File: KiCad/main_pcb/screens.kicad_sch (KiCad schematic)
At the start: 23 parts, among them U11 TI TXB0104DR, U12 ILI9488, U13 TI TXB0104DR, U14 SD Card Socket, U16 TI TXB0104DR

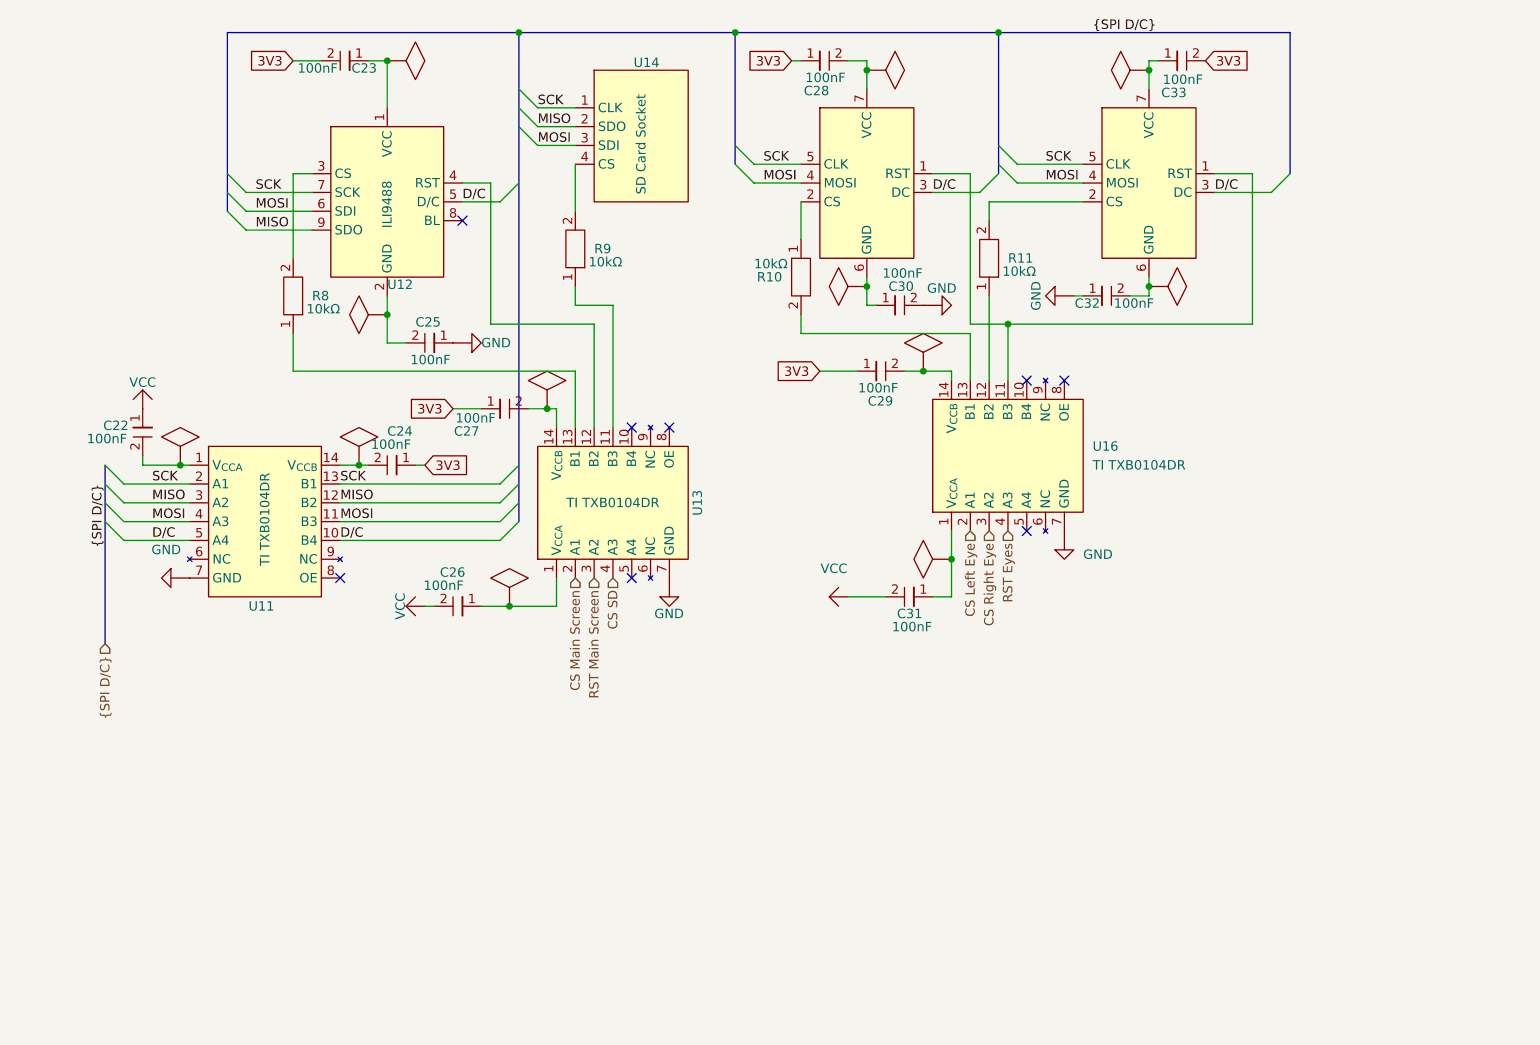
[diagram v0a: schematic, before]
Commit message: feat(KiCad): Adds parallel condensators for USB-C VBUS pin
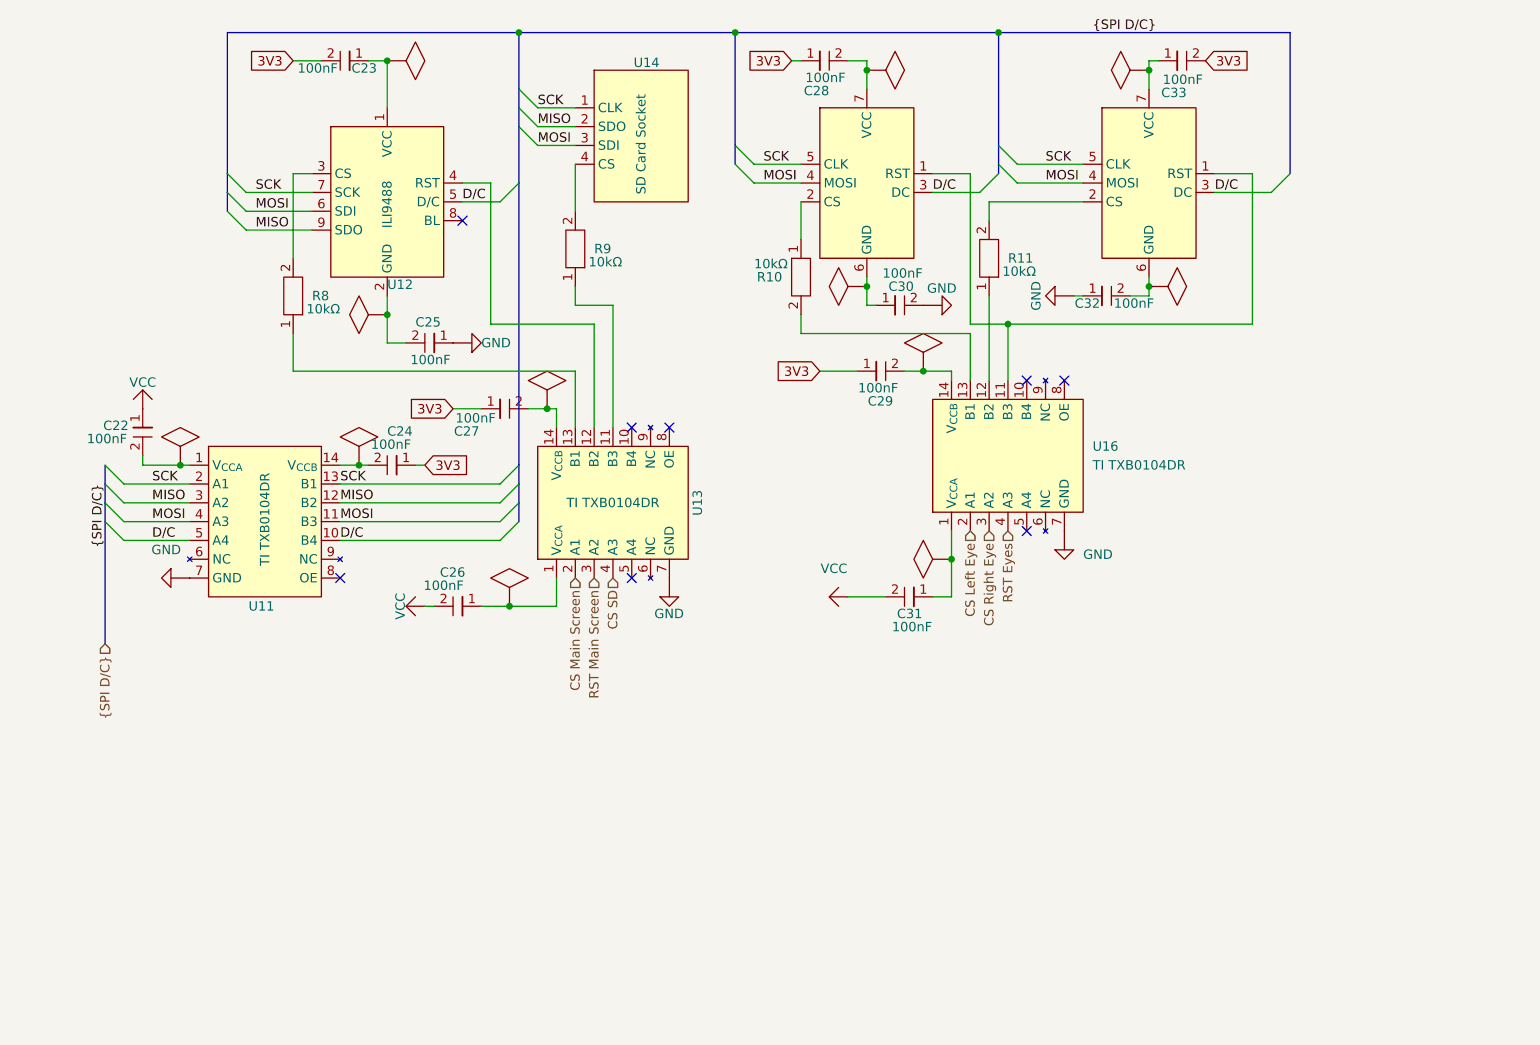
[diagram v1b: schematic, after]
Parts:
- U15, U17: value (none) -> ~

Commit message: feat(KiCad): Fixes symbols and ERC
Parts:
- C22, C23, C24, C25, C26, C27, C28, C29, C30, C31, C32, C33: symbol lilys_pad:Capacitor -> Lily's Pad:Capacitor
- R10, R11, R8, R9: symbol lilys_pad:Resistor -> Lily's Pad:Resistor
- U11, U13, U16: symbol lilys_pad:TI_TXB0104DR -> Lily's Pad:TI_TXB0104DR
- U12: symbol lilys_pad:ILI9488 -> Lily's Pad:ILI9488
- U14: symbol lilys_pad:SD_Card_Socket -> Lily's Pad:SD_Card_Socket
- U15, U17: symbol lilys_pad:GC9A01 -> Lily's Pad:GC9A01
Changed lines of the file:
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@@
 	)
 	(symbol
-		(lib_id "lilys_pad:Resistor")
+		(lib_id "Lily's Pad:Resistor")
 		(at 99.06 54.61 180)
 		(unit 1)
@@
 	)
 	(symbol
-		(lib_id "lilys_pad:PWR_FLG")
+		(lib_id "Lily's Pad:PWR_FLG")
 		(at 95.25 73.66 180)
 		(unit 1)
@@
 	)
 	(symbol
-		(lib_id "lilys_pad:Capacitor")
+		(lib_id "Lily's Pad:Capacitor")
 		(at 140.97 71.12 90)
 		(unit 1)
@@
 	)
 	(symbol
-		(lib_id "lilys_pad:GND")
+		(lib_id "Lily's Pad:GND")
 		(at 111.76 101.6 0)
 		(unit 1)
@@
 	)
 	(symbol
-		(lib_id "lilys_pad:Capacitor")
+		(lib_id "Lily's Pad:Capacitor")
 		(at 73.66 83.82 270)
 		(unit 1)
@@
 	)
 	(symbol
-		(lib_id "lilys_pad:PWR_FLG")
+		(lib_id "Lily's Pad:PWR_FLG")
 		(at 45.72 81.28 180)
 		(unit 1)
@@
 	)
 	(symbol
-		(lib_id "lilys_pad:TI_TXB0104DR")
+		(lib_id "Lily's Pad:TI_TXB0104DR")
 		(at 157.48 82.55 90)
 		(unit 1)
@@
 	)
 	(symbol
-		(lib_id "lilys_pad:GC9A01")
+		(lib_id "Lily's Pad:GC9A01")
 		(at 176.53 45.72 0)
 		(unit 1)
@@
 		)
 		(property "Value" "~"
-			(at 176.53 45.72 0)
-			(effects
-				(font
-					(size 1.27 1.27)
-				)
+			(at 178.6733 33.02 0)
+			(effects
+				(font
+					(size 1.27 1.27)
+				)
+				(justify left)
 			)
 		)
@@
 	)
 	(symbol
-		(lib_id "lilys_pad:VCC")
+		(lib_id "Lily's Pad:VCC")
 		(at 40.64 73.66 180)
 		(unit 1)
@@
 	)
 	(symbol
-		(lib_id "lilys_pad:Resistor")
+		(lib_id "Lily's Pad:Resistor")
 		(at 129.54 58.42 0)
 		(unit 1)
@@
 	)
 	(symbol
-		(lib_id "lilys_pad:PWR_FLG")
+		(lib_id "Lily's Pad:PWR_FLG")
 		(at 147.32 96.52 270)
 		(unit 1)
@@
 	)
 	(symbol
-		(lib_id "lilys_pad:Resistor")
+		(lib_id "Lily's Pad:Resistor")
 		(at 154.94 55.88 180)
 		(unit 1)
@@
 	)
 	(symbol
-		(lib_id "lilys_pad:Capacitor")
+		(lib_id "Lily's Pad:Capacitor")
 		(at 181.61 29.21 90)
 		(unit 1)
@@
 	)
 	(symbol
-		(lib_id "lilys_pad:Capacitor")
+		(lib_id "Lily's Pad:Capacitor")
 		(at 67.31 29.21 270)
 		(unit 1)
@@
 	)
 	(symbol
-		(lib_id "lilys_pad:Capacitor")
+		(lib_id "Lily's Pad:Capacitor")
 		(at 133.35 29.21 90)
 		(unit 1)
@@
 	)
 	(symbol
-		(lib_id "lilys_pad:PWR_FLG")
+		(lib_id "Lily's Pad:PWR_FLG")
 		(at 71.12 63.5 270)
 		(unit 1)
@@
 	)
 	(symbol
-		(lib_id "lilys_pad:PWR_FLG")
+		(lib_id "Lily's Pad:PWR_FLG")
 		(at 135.89 59.69 270)
 		(unit 1)
@@
 	)
 	(symbol
-		(lib_id "lilys_pad:GND")
+		(lib_id "Lily's Pad:GND")
 		(at 165.1 95.25 0)
 		(unit 1)
@@
 		)
 		(property "Value" "GND"
-			(at 167.64 95.8849 0)
-			(effects
-				(font
-					(size 1.27 1.27)
-				)
-				(justify left)
+			(at 165.1 99.06 0)
+			(effects
+				(font
+					(size 1.27 1.27)
+				)
 			)
 		)
@@
 	)
 	(symbol
-		(lib_id "lilys_pad:Capacitor")
+		(lib_id "Lily's Pad:Capacitor")
 		(at 143.51 101.6 270)
 		(unit 1)
@@
 	)
 	(symbol
-		(lib_id "lilys_pad:TI_TXB0104DR")
+		(lib_id "Lily's Pad:TI_TXB0104DR")
 		(at 57.15 91.44 0)
 		(unit 1)
@@
 	)
 	(symbol
-		(lib_id "lilys_pad:Capacitor")
+		(lib_id "Lily's Pad:Capacitor")
 		(at 90.17 76.2 90)
 		(unit 1)
@@
 	)
 	(symbol
-		(lib_id "lilys_pad:ILI9488")
+		(lib_id "Lily's Pad:ILI9488")
 		(at 73.66 48.26 0)
 		(unit 1)
@@
 	)
 	(symbol
-		(lib_id "lilys_pad:SD_Card_Socket")
+		(lib_id "Lily's Pad:SD_Card_Socket")
 		(at 107.95 39.37 0)
 		(unit 1)
@@
 	)
 	(symbol
-		(lib_id "lilys_pad:PWR_FLG")
+		(lib_id "Lily's Pad:PWR_FLG")
 		(at 146.05 68.58 180)
 		(unit 1)
@@
 	)
 	(symbol
-		(lib_id "lilys_pad:PWR_FLG")
+		(lib_id "Lily's Pad:PWR_FLG")
 		(at 69.85 81.28 180)
 		(unit 1)
@@
 	)
 	(symbol
-		(lib_id "lilys_pad:PWR_FLG")
+		(lib_id "Lily's Pad:PWR_FLG")
 		(at 140.97 30.48 90)
 		(unit 1)
@@
 	)
 	(symbol
-		(lib_id "lilys_pad:Capacitor")
+		(lib_id "Lily's Pad:Capacitor")
 		(at 78.74 67.31 270)
 		(unit 1)
@@
 	)
 	(symbol
-		(lib_id "lilys_pad:Capacitor")
+		(lib_id "Lily's Pad:Capacitor")
 		(at 82.55 102.87 270)
 		(unit 1)
@@
 	)
 	(symbol
-		(lib_id "lilys_pad:PWR_FLG")
+		(lib_id "Lily's Pad:PWR_FLG")
 		(at 173.99 30.48 270)
 		(unit 1)
@@
 	)
 	(symbol
-		(lib_id "lilys_pad:GC9A01")
+		(lib_id "Lily's Pad:GC9A01")
 		(at 138.43 45.72 0)
 		(unit 1)
@@
 		)
 		(property "Value" "~"
-			(at 138.43 45.72 0)
-			(effects
-				(font
-					(size 1.27 1.27)
-				)
+			(at 140.5733 33.02 0)
+			(effects
+				(font
+					(size 1.27 1.27)
+				)
+				(justify left)
 			)
 		)
@@
 	)
 	(symbol
-		(lib_id "lilys_pad:GND")
+		(lib_id "Lily's Pad:GND")
 		(at 163.83 60.96 270)
 		(unit 1)
@@
 	)
 	(symbol
-		(lib_id "lilys_pad:Capacitor")
+		(lib_id "Lily's Pad:Capacitor")
 		(at 171.45 60.96 90)
 		(unit 1)
@@
 	)
 	(symbol
-		(lib_id "lilys_pad:GND")
+		(lib_id "Lily's Pad:GND")
 		(at 85.09 67.31 90)
 		(unit 1)
@@
 	)
 	(symbol
-		(lib_id "lilys_pad:GND")
+		(lib_id "Lily's Pad:GND")
 		(at 44.45 99.06 270)
 		(unit 1)
@@
 		)
 		(property "Value" "GND"
-			(at 43.815 95.25 90)
-			(effects
-				(font
-					(size 1.27 1.27)
-				)
+			(at 41.91 99.0599 90)
+			(effects
+				(font
+					(size 1.27 1.27)
+				)
+				(justify right)
 			)
 		)
@@
 	)
 	(symbol
-		(lib_id "lilys_pad:VCC")
+		(lib_id "Lily's Pad:VCC")
 		(at 76.2 102.87 270)
 		(unit 1)
@@
 	)
 	(symbol
-		(lib_id "lilys_pad:Capacitor")
+		(lib_id "Lily's Pad:Capacitor")
 		(at 40.64 80.01 0)
 		(unit 1)
@@
 	)
 	(symbol
-		(lib_id "lilys_pad:PWR_FLG")
+		(lib_id "Lily's Pad:PWR_FLG")
 		(at 179.07 59.69 90)
 		(unit 1)
@@
 	)
 	(symbol
-		(lib_id "lilys_pad:PWR_FLG")
+		(lib_id "Lily's Pad:PWR_FLG")
 		(at 76.2 29.21 90)
 		(unit 1)
@@
 	)
 	(symbol
-		(lib_id "lilys_pad:TI_TXB0104DR")
+		(lib_id "Lily's Pad:TI_TXB0104DR")
 		(at 104.14 88.9 90)
 		(unit 1)
@@
 	)
 	(symbol
-		(lib_id "lilys_pad:Capacitor")
+		(lib_id "Lily's Pad:Capacitor")
 		(at 143.51 62.23 90)
 		(unit 1)
@@
 	)
 	(symbol
-		(lib_id "lilys_pad:VCC")
+		(lib_id "Lily's Pad:VCC")
 		(at 133.35 101.6 270)
 		(unit 1)
@@
 		)
 		(property "Value" "VCC"
-			(at 133.985 97.79 90)
-			(effects
-				(font
-					(size 1.27 1.27)
-				)
+			(at 132.08 101.5999 90)
+			(effects
+				(font
+					(size 1.27 1.27)
+				)
+				(justify right)
 			)
 		)
@@
 	)
 	(symbol
-		(lib_id "lilys_pad:GND")
+		(lib_id "Lily's Pad:GND")
 		(at 148.59 62.23 90)
 		(unit 1)
@@
 	)
 	(symbol
-		(lib_id "lilys_pad:Resistor")
+		(lib_id "Lily's Pad:Resistor")
 		(at 60.96 60.96 180)
 		(unit 1)
@@
 	)
 	(symbol
-		(lib_id "lilys_pad:PWR_FLG")
+		(lib_id "Lily's Pad:PWR_FLG")
 		(at 90.17 100.33 180)
 		(unit 1)

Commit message: feat(KiCad): Continues work
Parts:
- removed C25, C30, C32: 100nF, symbol Lily's Pad:Capacitor
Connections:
- net 3V3: now also U12.1 (VCC)
- net GND: now also C23.1, U12.2 (GND), U15.6 (GND), U17.6 (GND)
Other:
- moved on the sheet: C22, C23, C24, C26, C27, C28, C29, C31, C33, R10, R11, R8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

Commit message: feat(KiCad): Continues work
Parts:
- C22, C23, C24, C26, C27, C28, C29, C31, C33: footprint (none) -> Capacitor_SMD:C_0201_0603Metric_Pad0.64x0.40mm_HandSolder
- R10, R11, R8, R9: footprint (none) -> Resistor_SMD:R_0201_0603Metric_Pad0.64x0.40mm_HandSolder
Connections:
- net 3V3: now also C24.2, C27.2, C29.2, U11.14 (V_{CCB}), U13.14 (V_{CCB}), U15.7 (VCC), U16.14 (V_{CCB}), U17.7 (VCC); no longer C24.1, C27.1, C29.1
- net GND: now also C22.1, C24.1, C26.2, C27.1, C28.2, C29.1, C31.1, C33.1
- net VCC: now also C22.2, C26.1, U11.1 (V_{CCA}), U13.1 (V_{CCA}), U16.1 (V_{CCA}); no longer C22.1, C26.2
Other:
- moved on the sheet: C22, C24, C26, C27, C28, C29, C31, C33

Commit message: feat(KiCad): Continues work
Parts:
- added R12: 100Ω, Resistor_SMD:R_0201_0603Metric_Pad0.64x0.40mm_HandSolder, symbol Lily's Pad:Resistor
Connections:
- net VCC: now also R12.1
- net at U12.3 (CS): now also R8.1, R12.2; no longer R8.2
- net at U13.13 (B1): now also R8.2; no longer R8.1
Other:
- note added: "I don't even know if pull-up resistors are needed for CS pins since they're supposed to be driven HIGH when not used. But line has to be low when they are used, so I feel like I'd need a pull-down rather"
- moved on the sheet: R8
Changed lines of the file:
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@@
 	(generator_version "9.0")
 	(paper "A4")
+	(text "I don't even know if pull-up resistors are needed\nfor CS pins since they're supposed to be driven\nHIGH when not used. But line has to be low when\nthey are used, so I feel like I'd need a pull-down\nrather"
+		(exclude_from_sim no)
+		(at 23.368 82.55 0)
+		(effects
+			(font
+				(size 1.27 1.27)
+			)
+			(justify left)
+		)
+	)
 	(junction
 		(at 105.41 54.61)
@@
 	)
 	(junction
+		(at 92.71 81.28)
+		(diameter 0)
+		(color 0 0 0 0)
+	)
+	(junction
 		(at 120.65 128.27)
 		(diameter 0)
@@
 	(wire
 		(pts
-			(xy 92.71 91.44) (xy 92.71 96.52)
+			(xy 92.71 95.25) (xy 92.71 96.52)
 		)
 		(stroke
@@
 	(wire
 		(pts
+			(xy 92.71 81.28) (xy 92.71 85.09)
+		)
+		(stroke
+			(width 0)
+			(type default)
+		)
+	)
+	(wire
+		(pts
+			(xy 91.44 81.28) (xy 92.71 81.28)
+		)
+		(stroke
+			(width 0)
+			(type default)
+		)
+	)
+	(wire
+		(pts
 			(xy 167.64 54.61) (xy 170.18 54.61)
 		)
@@
 		(dnp no)
 		(property "Reference" "R9"
-			(at 133.35 80.0099 0)
+			(at 130.81 80.01 90)
 			(effects
 				(font
 					(size 1.27 1.27)
 				)
-				(justify right)
 			)
 		)
 		(property "Value" "10kΩ"
-			(at 134.874 81.788 0)
+			(at 134.62 80.01 0)
 			(effects
 				(font
@@
 	)
 	(symbol
+		(lib_id "Lily's Pad:VCC")
+		(at 78.74 81.28 270)
+		(unit 1)
+		(exclude_from_sim no)
+		(in_bom no)
+		(on_board no)
+		(dnp no)
+		(fields_autoplaced yes)
+		(property "Reference" "#PWR041"
+			(at 77.47 81.28 0)
+			(effects
+				(font
+					(size 1.27 1.27)
+				)
+				(hide yes)
+			)
+		)
+		(property "Value" "VCC"
+			(at 77.47 81.2799 90)
+			(effects
+				(font
+					(size 1.27 1.27)
+				)
+				(justify right)
+			)
+		)
+		(property "Footprint" ""
+			(at 78.74 81.28 0)
+			(effects
+				(font
+					(size 1.27 1.27)
+				)
+				(hide yes)
+			)
+		)
+		(property "Datasheet" ""
+			(at 78.74 81.28 0)
+			(effects
+				(font
+					(size 1.27 1.27)
+				)
+				(hide yes)
+			)
+		)
+		(property "Description" ""
+			(at 78.74 81.28 0)
+			(effects
+				(font
+					(size 1.27 1.27)
+				)
+				(hide yes)
+			)
+		)
+		(pin "1"
+		)
+		(instances
+			(project "main_pcb"
+				(path "/346fb29b-2426-4b69-9f9a-e979b6e41832/f366ed97-9aa9-4dab-9fc7-1cd4f5d408d4"
+					(reference "#PWR041")
+					(unit 1)
+				)
+			)
+		)
+	)
+	(symbol
 		(lib_id "Lily's Pad:Capacitor")
 		(at 104.14 105.41 0)
@@
 		(dnp no)
 		(property "Reference" "C24"
-			(at 99.568 105.41 90)
+			(at 100.076 105.156 0)
 			(effects
 				(font
 					(size 1.27 1.27)
 				)
-				(justify left)
+				(justify right)
 			)
 		)
 		(property "Value" "100nF"
-			(at 101.346 104.902 90)
+			(at 99.568 103.378 0)
 			(effects
 				(font
@@
 	)
 	(symbol
+		(lib_id "Lily's Pad:Resistor")
+		(at 86.36 81.28 90)
+		(unit 1)
+		(exclude_from_sim no)
+		(in_bom yes)
+		(on_board yes)
+		(dnp no)
+		(property "Reference" "R12"
+			(at 86.36 81.28 90)
+			(effects
+				(font
+					(size 1.27 1.27)
+				)
+			)
+		)
+		(property "Value" "100Ω"
+			(at 86.36 83.566 90)
+			(effects
+				(font
+					(size 1.27 1.27)
+				)
+			)
+		)
+		(property "Footprint" "Resistor_SMD:R_0201_0603Metric_Pad0.64x0.40mm_HandSolder"
+			(at 86.36 81.28 0)
+			(effects
+				(font
+					(size 1.27 1.27)
+				)
+				(hide yes)
+			)
+		)
+		(property "Datasheet" ""
+			(at 86.36 81.28 0)
+			(effects
+				(font
+					(size 1.27 1.27)
+				)
+				(hide yes)
+			)
+		)
+		(property "Description" ""
+			(at 86.36 81.28 0)
+			(effects
+				(font
+					(size 1.27 1.27)
+				)
+				(hide yes)
+			)
+		)
+		(pin "2"
+		)
+		(pin "1"
+		)
+		(instances
+			(project "main_pcb"
+				(path "/346fb29b-2426-4b69-9f9a-e979b6e41832/f366ed97-9aa9-4dab-9fc7-1cd4f5d408d4"
+					(reference "R12")
+					(unit 1)
+				)
+			)
+		)
+	)
+	(symbol
 		(lib_id "Lily's Pad:GC9A01")
 		(at 208.28 71.12 0)
@@
 		(dnp no)
 		(property "Reference" "R10"
-			(at 158.75 83.8201 0)
+			(at 161.29 82.042 90)
 			(effects
 				(font
@@
 		)
 		(property "Value" "10kΩ"
-			(at 157.226 82.042 0)
+			(at 165.1 83.82 0)
 			(effects
 				(font
@@
 		(dnp no)
 		(property "Reference" "R11"
-			(at 189.23 81.2799 0)
+			(at 186.69 83.312 90)
 			(effects
 				(font
@@
 		)
 		(property "Value" "10kΩ"
-			(at 190.754 83.058 0)
+			(at 190.5 81.28 0)
 			(effects
 				(font
@@
 		(dnp no)
 		(property "Reference" "C26"
-			(at 116.078 135.128 90)
+			(at 125.73 133.604 0)
 			(effects
 				(font
 					(size 1.27 1.27)
 				)
-				(justify left)
+				(justify right)
 			)
 		)
 		(property "Value" "100nF"
-			(at 117.856 134.62 90)
+			(at 125.222 131.826 0)
 			(effects
 				(font
@@
 	(symbol
 		(lib_id "Lily's Pad:Resistor")
-		(at 92.71 86.36 180)
+		(at 92.71 90.17 0)
 		(unit 1)
 		(exclude_from_sim no)
@@
 		(dnp no)
 		(property "Reference" "R8"
-			(at 95.25 86.3599 0)
+			(at 92.71 88.9 90)
 			(effects
 				(font
@@
 		)
 		(property "Value" "10kΩ"
-			(at 96.774 88.138 0)
+			(at 96.52 90.17 0)
 			(effects
 				(font
@@
 		)
 		(property "Footprint" "Resistor_SMD:R_0201_0603Metric_Pad0.64x0.40mm_HandSolder"
-			(at 92.71 86.36 0)
+			(at 92.71 90.17 0)
 			(effects
 				(font
@@
 		)
 		(property "Datasheet" ""
-			(at 92.71 86.36 0)
+			(at 92.71 90.17 0)
 			(effects
 				(font
@@
 		)
 		(property "Description" ""
-			(at 92.71 86.36 0)
+			(at 92.71 90.17 0)
 			(effects
 				(font

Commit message: feat(KiCad): Continues work
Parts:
- removed C23: 100nF, Capacitor_SMD:C_0201_0603Metric_Pad0.64x0.40mm_HandSolder, symbol Lily's Pad:Capacitor
- removed R12: 100Ω, Resistor_SMD:R_0201_0603Metric_Pad0.64x0.40mm_HandSolder, symbol Lily's Pad:Resistor
- added C14: 100nF, Capacitor_SMD:C_0201_0603Metric_Pad0.64x0.40mm_HandSolder, symbol Lily's Pad:Capacitor
- renumbered C22 to C12, C24 to C13, C27 to C15, C26 to C16, C29 to C17, C31 to C18, C28 to C19, C33 to C20, U17 to U10, U11 to U4, U12 to U5, U13 to U6, U14 to U7, U15 to U8, U16 to U9
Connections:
- net 3V3: now also C15.1, C14.1; no longer C15.2
- net CS SD: now also U6.5 (A4); no longer U6.4 (A3)
- net GND: now also C15.2, C14.2; no longer C15.1
- net RST Main Screen: now also U6.4 (A3); no longer U6.3 (A2)
- net at R9.1: now also U6.10 (B4); no longer U6.11 (B3)
- net at U5.4 (RST): now also U6.11 (B3); no longer U6.12 (B2)
- net at U5.8 (BL): now also U6.12 (B2)
- no-connect marks 8 -> 5
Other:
- note added: "TODO: VCC or dedicated MCU pin"
- moved on the sheet: U4, U5, U6, U7
